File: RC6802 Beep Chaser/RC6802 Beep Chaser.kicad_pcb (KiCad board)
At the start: 2 copper layers, 99.1 x 78.8 mm, 25 parts, among them J2 RC6802_UI_Port, M3 Mounting, M4 Mounting, U1 74LS374, U2 74LS374

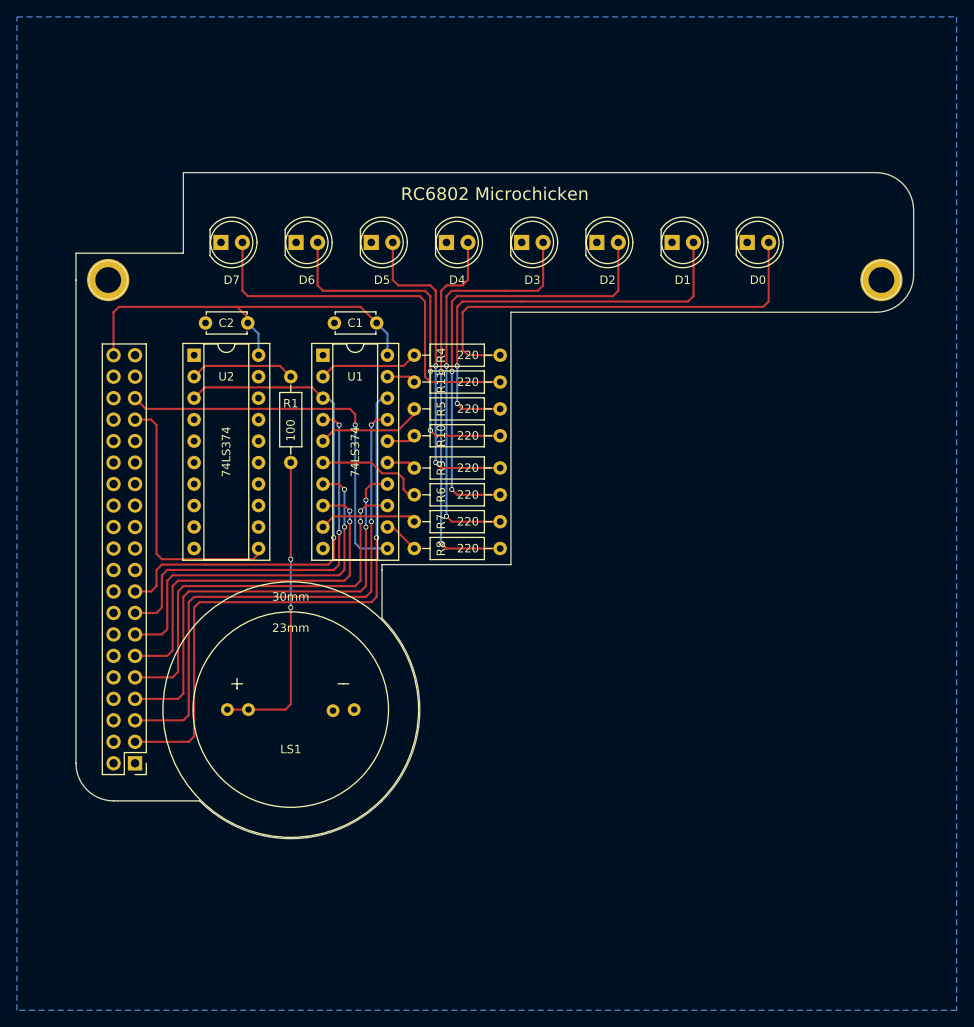
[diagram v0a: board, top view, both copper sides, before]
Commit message: Latch beep chaser outputs on write only
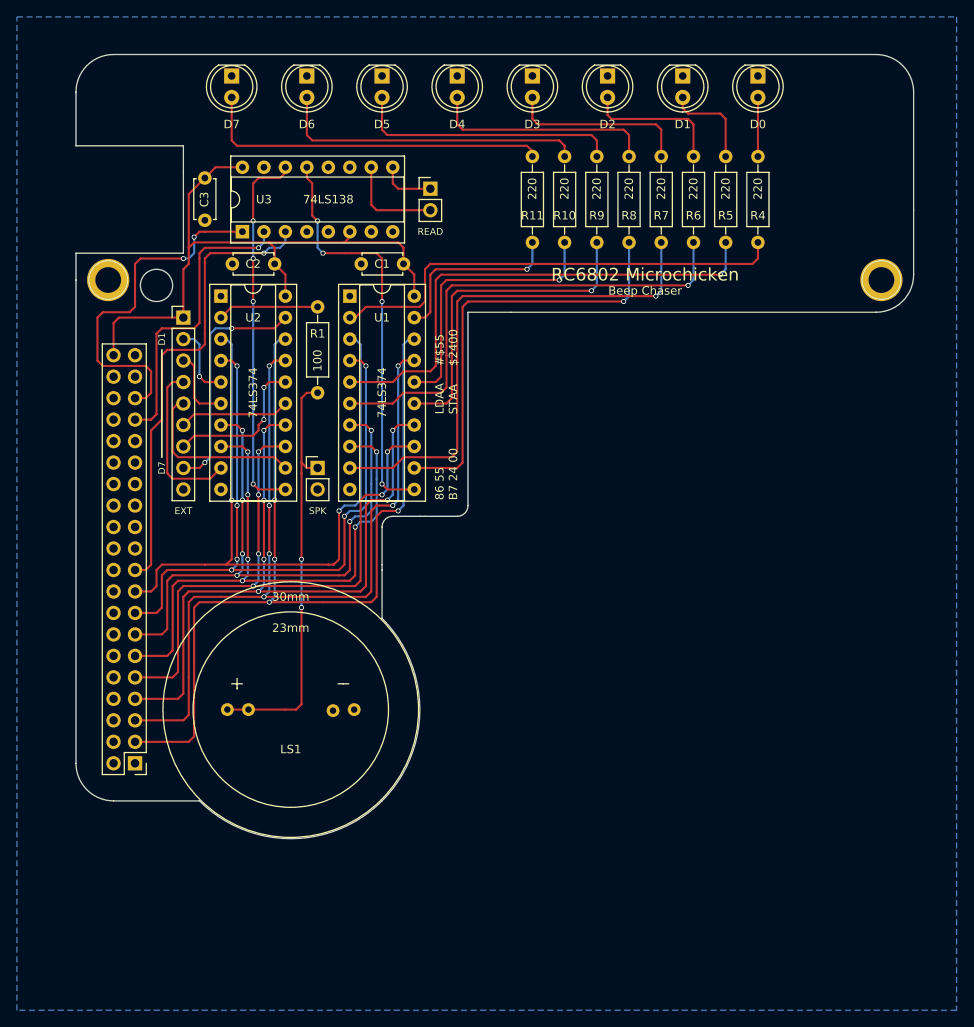
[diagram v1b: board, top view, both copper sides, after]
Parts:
- added C3: 100nF, Capacitors_THT:C_Disc_D4.7mm_W2.5mm_P5.00mm, F.Cu at (115.6, 62.9)
- added J1: SPK, Pin_Headers:Pin_Header_Straight_1x02_Pitch2.54mm, F.Cu at (128.9, 97.2)
- added J3: EXT, Pin_Headers:Pin_Header_Straight_1x09_Pitch2.54mm, F.Cu at (113.0, 79.4)
- added J4: READ, Pin_Headers:Pin_Header_Straight_1x02_Pitch2.54mm, F.Cu at (142.2, 64.1)
- added U3: 74LS138, Housings_DIP:DIP-16_W7.62mm_Socket, F.Cu at (120.0, 69.2)
- moved R8 48.8 mm to (165.7, 60.3), turned to 270 degrees
- moved R7 47.2 mm to (169.5, 60.3), turned to 270 degrees
- moved R6 46.1 mm to (173.4, 60.3), turned to 270 degrees
- moved R5 40.0 mm to (177.2, 60.3), turned to 270 degrees
- moved R9 38.6 mm to (161.9, 60.3), turned to 270 degrees
- moved R4 38.5 mm to (181.0, 60.3), turned to 270 degrees
- moved R10 33.9 mm to (158.1, 60.3), turned to 270 degrees
- moved R11 26.9 mm to (154.3, 60.3), turned to 270 degrees
- moved D0 19.7 mm to (181.0, 50.8), turned to 270 degrees
- moved D1 19.7 mm to (172.1, 50.8), turned to 270 degrees
- moved D2 19.7 mm to (163.2, 50.8), turned to 270 degrees
- moved D3 19.7 mm to (154.3, 50.8), turned to 270 degrees
- moved D4 19.7 mm to (145.4, 50.8), turned to 270 degrees
- moved D5 19.7 mm to (136.5, 50.8), turned to 270 degrees
- moved D6 19.7 mm to (127.6, 50.8), turned to 270 degrees
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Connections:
- J2 pad 19: (no net) -> /R/~W
- U1 pad 11: /IO1 -> IO1_W
- U2 pad 11: /IO2 -> IO2_W
- U2 pad 12: (no net) -> Net-(J3-Pad5)
- U2 pad 13: GND -> /D4
- U2 pad 14: GND -> /D5
- U2 pad 15: (no net) -> Net-(J3-Pad6)
- U2 pad 16: (no net) -> Net-(J3-Pad7)
- U2 pad 17: GND -> /D6
- U2 pad 18: GND -> /D7
- U2 pad 19: (no net) -> Net-(J3-Pad8)
- U2 pad 4: GND -> /D1
- U2 pad 5: (no net) -> Net-(J3-Pad2)
- U2 pad 6: (no net) -> Net-(J3-Pad3)
- U2 pad 7: GND -> /D2
- U2 pad 8: GND -> /D3
- U2 pad 9: (no net) -> Net-(J3-Pad4)
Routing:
- net /R/~W: track 0.00 -> 54.8 mm, vias 0 -> 1
- net Net-(R7-Pad2): track 11.6 -> 61.6 mm, vias 0 -> 1
- net IO1_W: track 0.00 -> 48.9 mm, vias 0 -> 4
- net Net-(R8-Pad2): track 4.23 -> 51.0 mm, vias 0 -> 1
- net Net-(R5-Pad2): track 12.7 -> 59.1 mm, vias 0 -> 1
- net Net-(D0-Pad2): track 52.9 -> 6.98 mm
- net Net-(R6-Pad2): track 13.1 -> 57.8 mm, vias 0 -> 1
- net IO2_W: track 0.00 -> 44.6 mm, vias 0 -> 4
- net Net-(R4-Pad2): track 11.8 -> 55.3 mm
- net /D7: track 69.0 -> 110.7 mm, vias 1 -> 4
- net Net-(D1-Pad2): track 51.6 -> 11.3 mm, vias 2 -> 0
- net /D6: track 63.9 -> 103.1 mm, vias 2 -> 6
- net Net-(D2-Pad2): track 54.1 -> 16.5 mm, vias 2 -> 0
- net Net-(R9-Pad2): track 3.44 -> 39.5 mm, vias 0 -> 1
- net /D1: track 47.4 -> 83.4 mm, vias 2 -> 6
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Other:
- board size 99.1 x 78.8 mm -> 99.1 x 92.7 mm
- board text added: "#$55 $2400"
- board text added: "$2400"
- board text added: "$2800"
- board text added: "86 55 B7 24 00"
- board text added: "D1"
- board text added: "D7"
- board text added: "DEVICE DECODING"
- board text added: "LDAA STAA"
- board text added: "OUTPUT LATCH"
- board text added: "Revision B"
- board text removed: "Revision A"

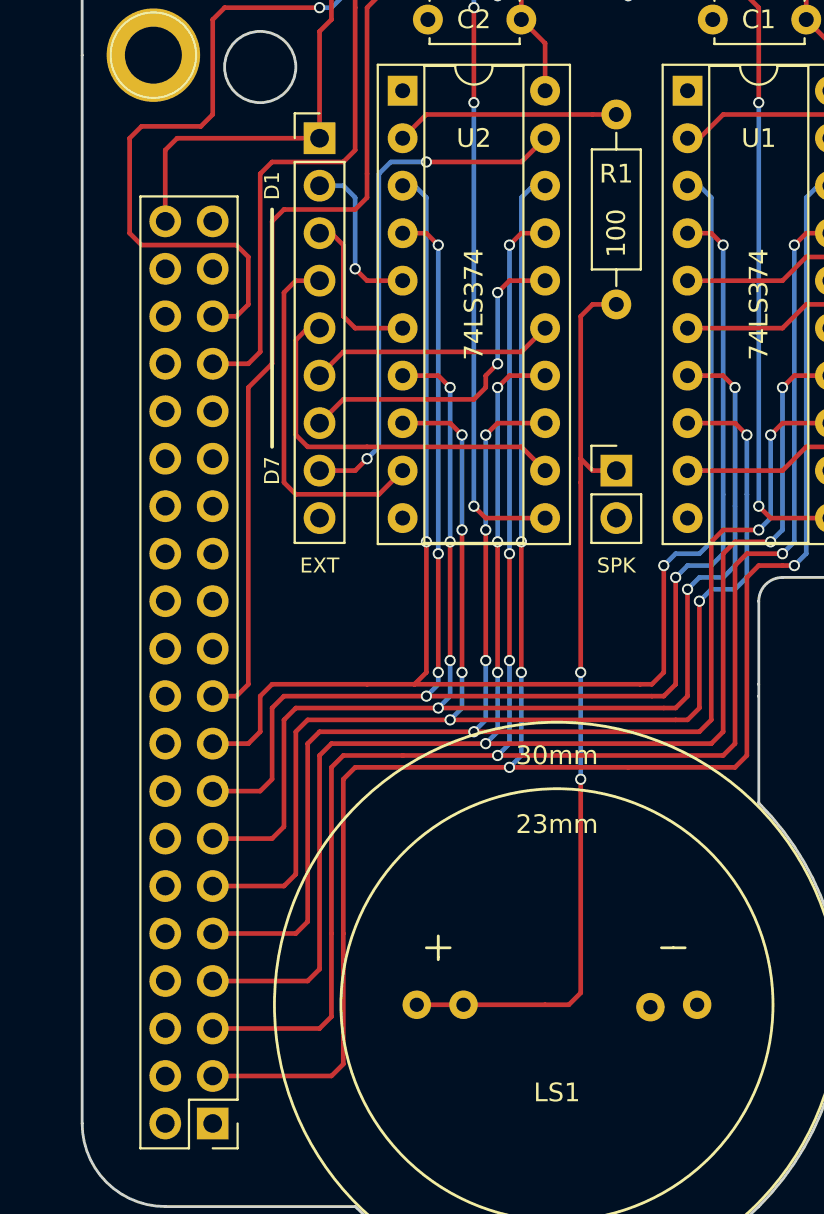
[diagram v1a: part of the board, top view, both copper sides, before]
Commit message: Added transistor to drive speaker
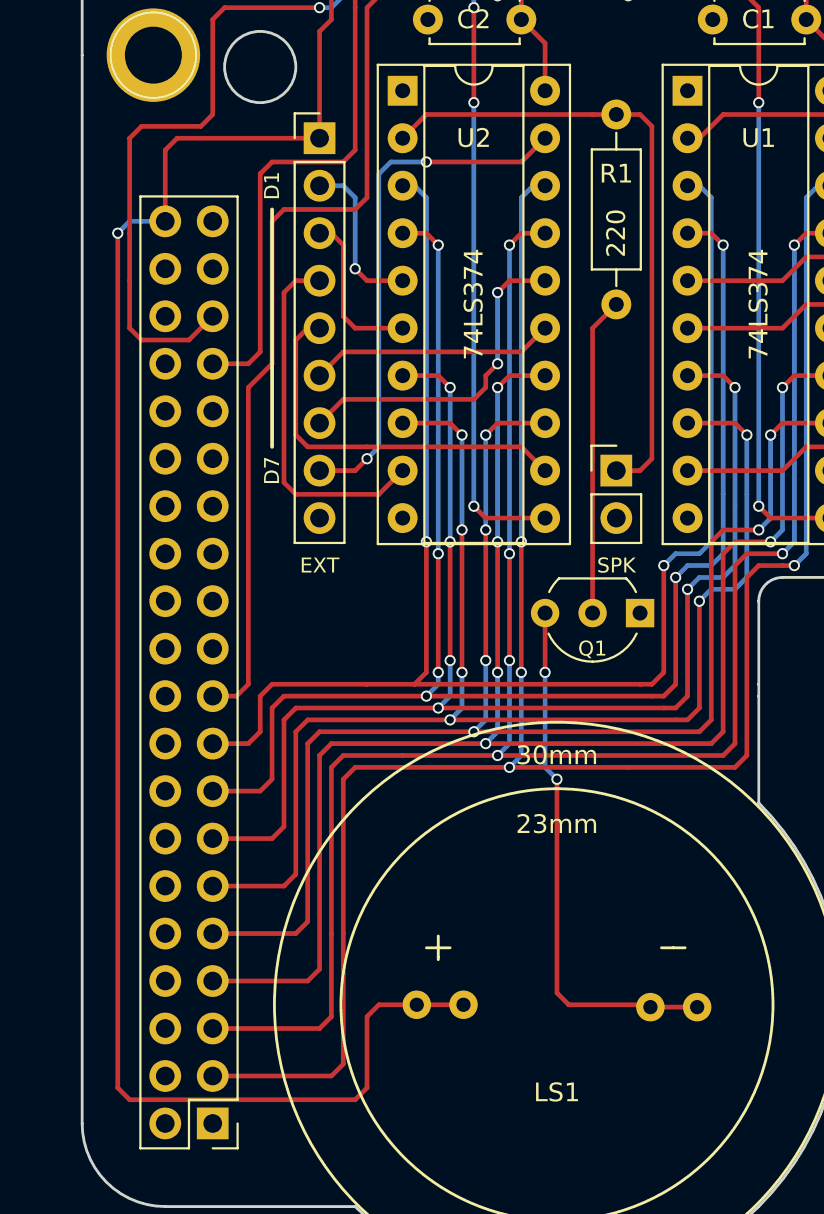
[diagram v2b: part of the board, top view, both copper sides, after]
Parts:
- added Q1: 2N3904, TO_SOT_Packages_THT:TO-92_Inline_Wide, F.Cu at (130.2, 104.8)
- R1: value 100 -> 220
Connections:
- LS1 pad 1: Net-(J1-Pad1) -> VCC
- LS1 pad 2: GND -> Net-(LS1-Pad2)
- R1 pad 1: Net-(J1-Pad1) -> Net-(Q1-Pad2)
- R1 pad 2: Net-(R1-Pad2) -> Net-(J1-Pad1)
- U2 pad 2: Net-(R1-Pad2) -> Net-(J1-Pad1)
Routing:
- net VCC: track 77.2 -> 148.9 mm, vias 0 -> 1
- net Net-(LS1-Pad2): track 0.00 -> 28.4 mm, vias 0 -> 2
- net Net-(Q1-Pad2): track 0.00 -> 17.0 mm
- net Net-(J1-Pad1): track 49.6 -> 34.1 mm, vias 2 -> 0
- net Net-(R1-Pad2): track 12.0 -> 0.00 mm
- net /IO1: track 42.1 -> 41.5 mm
